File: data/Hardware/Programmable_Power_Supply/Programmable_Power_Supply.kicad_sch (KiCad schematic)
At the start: 1 part, among them U1 STM32G431CBT6

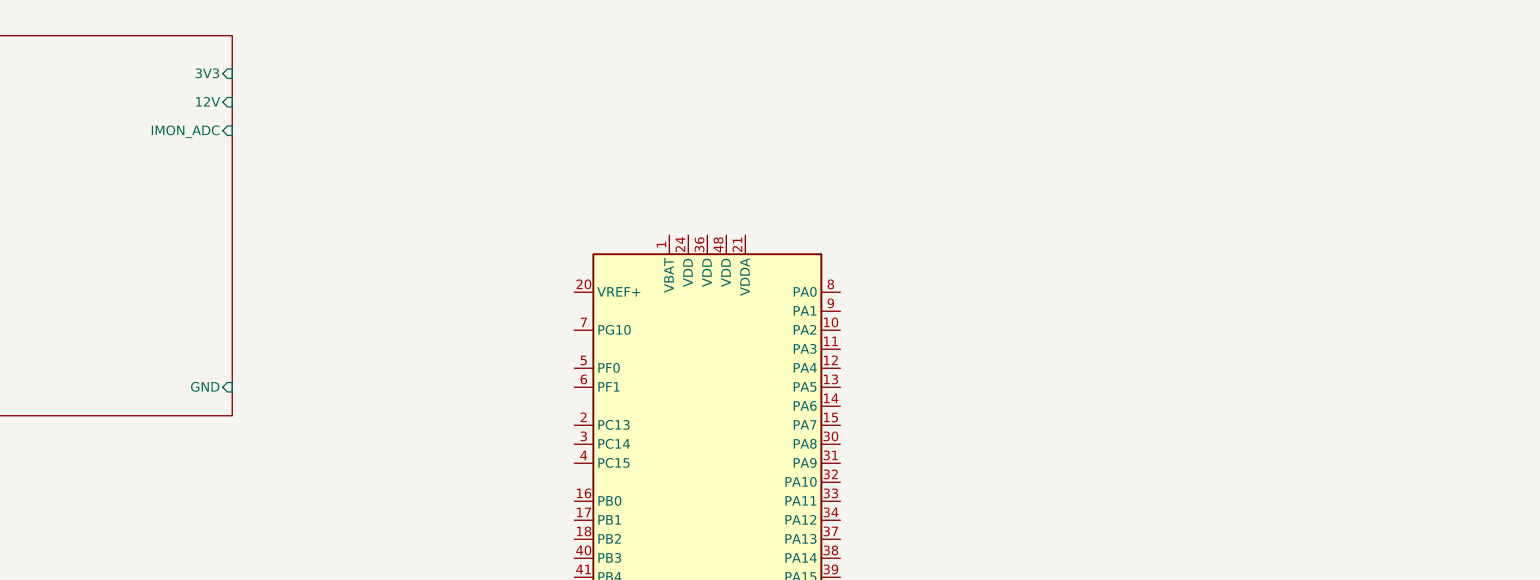
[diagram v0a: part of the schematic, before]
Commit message: feat: Adding output section to the schematic.
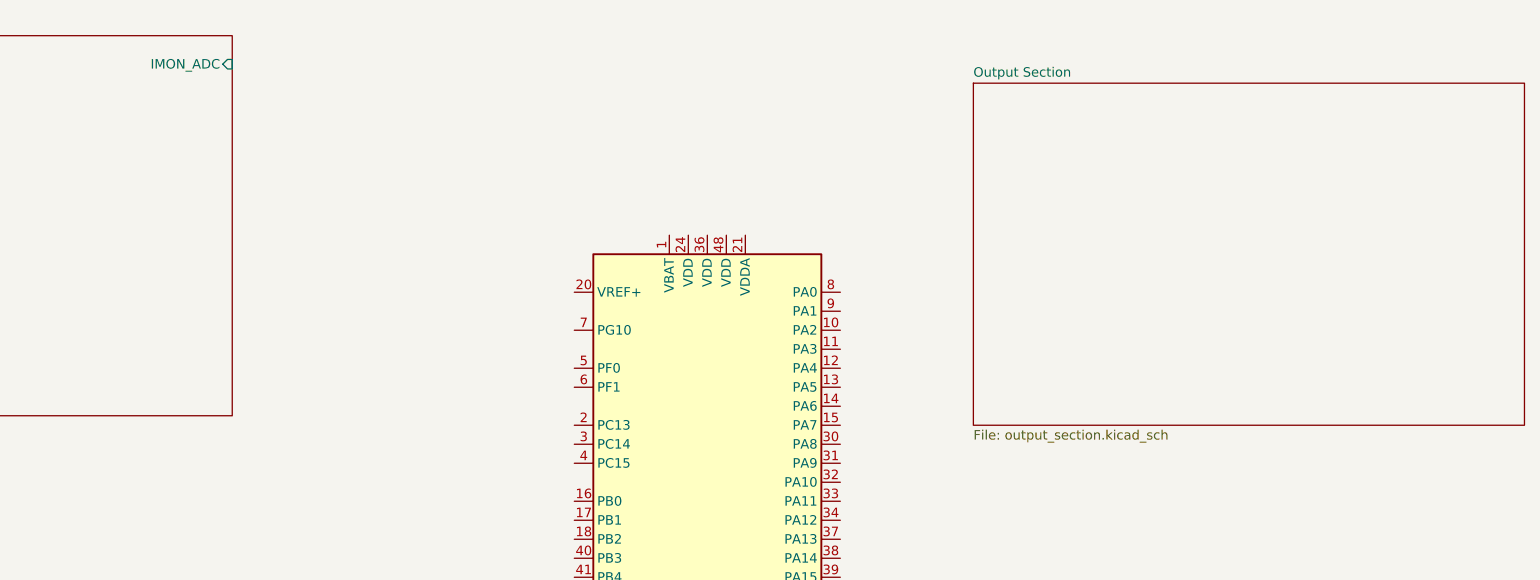
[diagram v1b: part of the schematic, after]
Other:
- added sheet Output Section (output_section.kicad_sch)
- sheet Input Section ports: added none; removed 12V, 3V3, GND
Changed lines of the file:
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@@
+	)
+	(sheet
+		(at 203.2 27.94)
+		(size 73.66 45.72)
+		(exclude_from_sim no)
+		(in_bom yes)
+		(on_board yes)
+		(dnp no)
+		(fields_autoplaced yes)
+		(stroke
+			(width 0.1524)
+			(type solid)
+		)
+		(fill
+			(color 0 0 0 0.0000)
+		)
+		(property "Sheetname" "Output Section"
+			(at 203.2 27.2284 0)
+			(effects
+				(font
+					(size 1.27 1.27)
+				)
+				(justify left bottom)
+			)
+		)
+		(property "Sheetfile" "output_section.kicad_sch"
+			(at 203.2 74.2446 0)
+			(effects
+				(font
+					(size 1.27 1.27)
+				)
+				(justify left top)
+			)
+		)
+		(instances
+			(project "Programmable_Power_Supply"
+				(path "/b54e5edd-9bd1-4c5e-a8c2-662f0aedeac0"
+					(page "3")
+				)
+			)
+		)
 	)
 	(sheet
@@
 			)
 		)
-		(pin "3V3" input
-			(at 104.14 26.67 0)
+		(pin "IMON_ADC" input
+			(at 104.14 25.4 0)
 			(effects
 				(font
-					(size 1.27 1.27)
-				)
-				(justify right)
-			)
-		)
-		(pin "12V" input
-			(at 104.14 30.48 0)
-			(effects
-				(font
-					(size 1.27 1.27)
-				)
-				(justify right)
-			)
-		)
-		(pin "GND" input
-			(at 104.14 68.58 0)
-			(effects
-				(font
-					(size 1.27 1.27)
-				)
-				(justify right)
-			)
-		)
-		(pin "IMON_ADC" input
-			(at 104.14 34.29 0)
-			(effects
-				(font

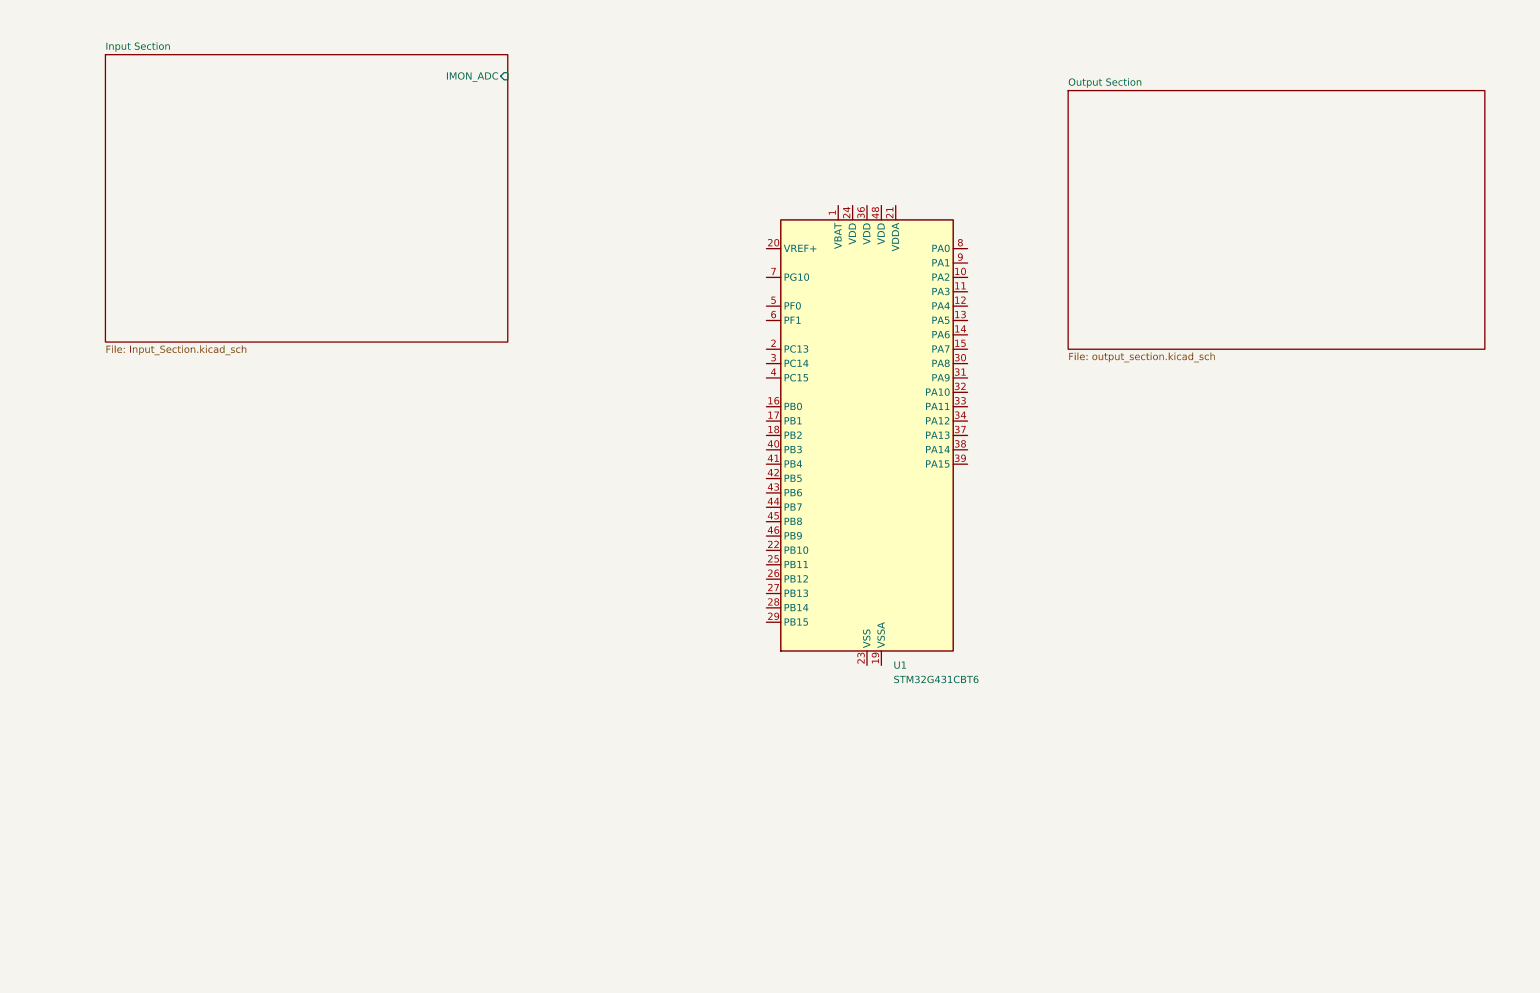
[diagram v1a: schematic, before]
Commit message: feat: First draw of full schematic with all footprints and symbols.
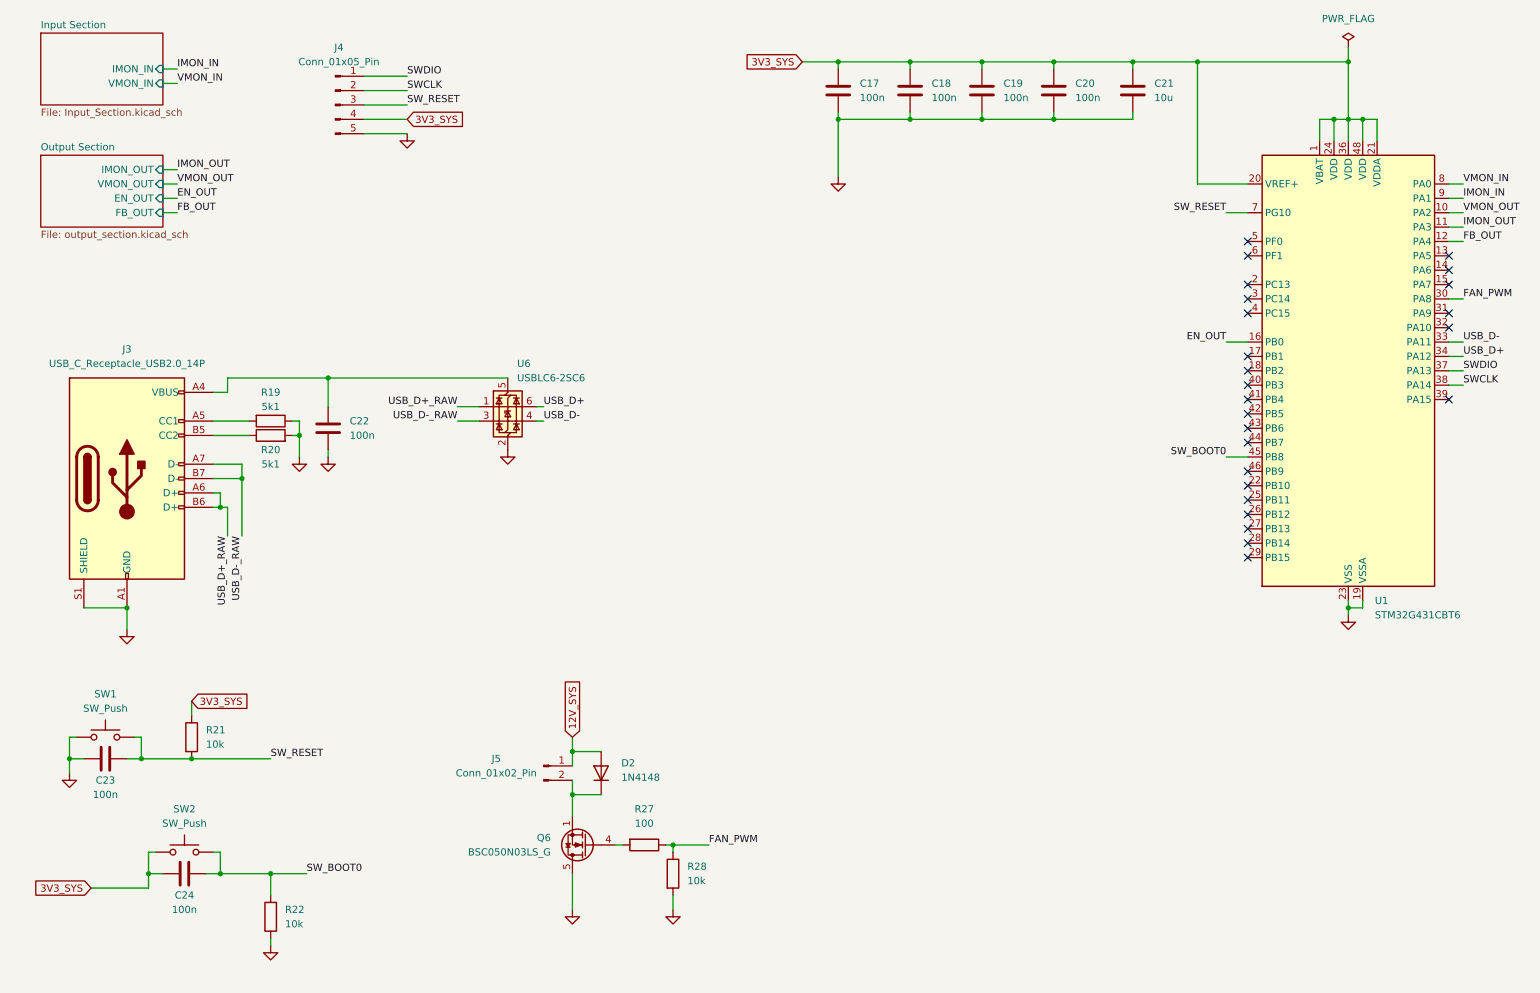
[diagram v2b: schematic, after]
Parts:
- added C17, C18, C19, C20, C22, C23, C24: 100n, Capacitor_SMD:C_0805_2012Metric_Pad1.18x1.45mm_HandSolder, symbol Device:C
- added C21: 10u, Capacitor_SMD:C_1206_3216Metric_Pad1.33x1.80mm_HandSolder, symbol Device:C
- added D2: 1N4148, Diode_THT:D_DO-35_SOD27_P7.62mm_Horizontal, symbol Diode:1N4148
- added J3: USB_C_Receptacle_USB2.0_14P, Connector_USB:USB_C_Receptacle_HRO_TYPE-C-31-M-12, symbol Connector:USB_C_Receptacle_USB2.0_14P
- added J4: Conn_01x05_Pin, Connector_PinHeader_2.54mm:PinHeader_1x05_P2.54mm_Vertical, symbol Connector:Conn_01x05_Pin
- added J5: Conn_01x02_Pin, Connector_Molex:Molex_KK-254_AE-6410-02A_1x02_P2.54mm_Vertical, symbol Connector:Conn_01x02_Pin
- added Q6: BSC050N03LS_G, Package_SON:Infineon_PG-TDSON-8_6.15x5.15mm, symbol Szymon_Piorun_library:BSC050N03LS_G
- added R19, R20: 5k1, Resistor_SMD:R_0603_1608Metric_Pad0.98x0.95mm_HandSolder, symbol Device:R
- added R21, R22, R28: 10k, Resistor_SMD:R_0603_1608Metric_Pad0.98x0.95mm_HandSolder, symbol Device:R
- added R27: 100, Resistor_SMD:R_0603_1608Metric_Pad0.98x0.95mm_HandSolder, symbol Device:R
- added SW1, SW2: SW_Push, Button_Switch_SMD:SW_Push_1P1T_NO_CK_KSC6xxG, symbol Switch:SW_Push
- added U6: USBLC6-2SC6, Package_TO_SOT_SMD:SOT-23-6, symbol Power_Protection:USBLC6-2SC6
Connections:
- net 3V3_SYS: now reaches U1.1 (VBAT)
- net 3V3_SYS: now also U1.20 (VREF+), U1.21 (VDDA), U1.24 (VDD), U1.36 (VDD), U1.48 (VDD), C17.1, C18.1, C19.1, C20.1, C21.1, C24.2, J4.4 (Pin_4), R21.1, SW2.1
- net VMON_OUT: now reaches U1.10 (PA2)
- net IMON_OUT: now reaches U1.11 (PA3)
- net FB_OUT: now reaches U1.12 (PA4)
- net EN_OUT: now reaches U1.16 (PB0)
- net GND: now reaches U1.19 (VSSA)
- net GND: now also U1.23 (VSS), U1.35 (VSS), U1.47 (VSS), C17.2, C18.2, C19.2, C20.2, C21.2, C22.2, C23.2, J3.A1 (GND), J3.A12 (GND), J3.B1 (GND), J3.B12 (GND), J3.S1 (SHIELD), J4.5 (Pin_5), Q6.5 (D), Q6.6 (D), Q6.7 (D), Q6.8 (D), R19.1, R20.2, R22.1, R28.2, SW1.1, U6.2 (GND)
- net FAN_PWM: now reaches U1.30 (PA8)
- net FAN_PWM: now also R27.1, R28.1
- net USB_D-: now reaches U1.33 (PA11)
- net USB_D-: now also U6.4 (I/O2)
- net USB_D+: now reaches U1.34 (PA12)
- net USB_D+: now also U6.6 (I/O1)
- net SWDIO: now reaches U1.37 (PA13)
- net SWDIO: now also J4.1 (Pin_1)
- net SWCLK: now reaches U1.38 (PA14)
- net SWCLK: now also J4.2 (Pin_2)
- net SW_BOOT0: now reaches U1.45 (PB8)
- net SW_BOOT0: now also C24.1, R22.2, SW2.2
- net SW_RESET: now reaches U1.7 (PG10)
- net SW_RESET: now also C23.1, J4.3 (Pin_3), R21.2, SW1.2
- net VMON_IN: now reaches U1.8 (PA0)
- net IMON_IN: now reaches U1.9 (PA1)
- new net: C22.1, J3.A4 (VBUS), J3.A9 (VBUS), J3.B4 (VBUS), J3.B9 (VBUS), U6.5 (VBUS)
- new net: J3.A5 (CC1), R19.2
- new net: D2.1 (K), J5.2 (Pin_2), Q6.1 (S), Q6.2 (S), Q6.3 (S)
- new net: Q6.4 (G), R27.2
- new net: J3.B5 (CC2), R20.1
- new net 12V_SYS: D2.2 (A), J5.1 (Pin_1)
- new net USB_D+_RAW: J3.A6 (D+), J3.B6 (D+), U6.1 (I/O1)
- new net USB_D-_RAW: J3.A7 (D-), J3.B7 (D-), U6.3 (I/O2)
- no-connect marks 0 -> 25
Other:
- sheet Input Section ports: added IMON_IN, VMON_IN; removed IMON_ADC
- sheet Output Section ports: added EN_OUT, FB_OUT, IMON_OUT, VMON_OUT; removed none
- moved on the sheet: U1

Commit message: feat: Final version of revision A of the schematic with mouser product numbers attached.
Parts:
- removed J3: USB_C_Receptacle_USB2.0_14P, Connector_USB:USB_C_Receptacle_HRO_TYPE-C-31-M-12, symbol Connector:USB_C_Receptacle_USB2.0_14P
- added J6: USB_C_Receptacle_USB2.0_16P, Connector_USB:USB_C_Receptacle_GCT_USB4105-xx-A_16P_TopMnt_Horizontal, symbol Connector:USB_C_Receptacle_USB2.0_16P
- C17, C18, C19, C20, C22, C23, C24: footprint Capacitor_SMD:C_0805_2012Metric_Pad1.18x1.45mm_HandSolder -> Capacitor_SMD:C_0201_0603Metric_Pad0.64x0.40mm_HandSolder; Mouser (none) -> MLASG063SB5104KFNA01
- C21: Mouser (none) -> GXT31CR6YA106KE01L
- D2: footprint Diode_THT:D_DO-35_SOD27_P7.62mm_Horizontal -> Szymon_Piorun_Library:SOD323; Mouser (none) -> 1N4148WS-HE3_A-18
- J4: now left out of the parts list
- J5: Mouser (none) -> 22-23-2021
- Q6: footprint Package_SON:Infineon_PG-TDSON-8_6.15x5.15mm -> Szymon_Piorun_Library:Infineon_PG-TDSON-8_6.15x5.15mm; Mouser (none) -> BSC030N03LS G
- R19, R20: Mouser (none) -> CR0603-FX-5101ELF
- R21, R22, R28: Mouser (none) -> RCA060310K0FKEC
- R27: Mouser (none) -> RT0603BRB07100RL
- SW1, SW2: footprint Button_Switch_SMD:SW_Push_1P1T_NO_CK_KSC6xxG -> Szymon_Piorun_Library:TS046650BK100SMTTR; Mouser (none) -> TS04-66-50-BK-100-SMT-TR
- U1: Mouser (none) -> STM32G431CBT6
- U6: Mouser (none) -> USBLC6-2SC6
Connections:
- net GND: now also C23.1, R20.1, R22.2, J6.A1 (GND), J6.A12 (GND), J6.B1 (GND), J6.B12 (GND), J6.S1 (SHIELD); no longer C23.2, R20.2, R22.1
- net SW_BOOT0: now also R22.1; no longer R22.2
- net SW_RESET: now also C23.2; no longer C23.1
- net USB_D+_RAW: now also J6.A6 (D+), J6.B6 (D+)
- net USB_D-_RAW: now also J6.A7 (D-), J6.B7 (D-)
- net at C22.1, U6.5 (VBUS): now also J6.A4 (VBUS), J6.A9 (VBUS), J6.B4 (VBUS), J6.B9 (VBUS)
- net at R19.2: now also J6.A5 (CC1)
- new net: J6.B5 (CC2), R20.2
- no-connect marks 25 -> 27

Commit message: feat: First full layout of the PCB
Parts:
- added H1, H2, H3, H4: MH, MountingHole:MountingHole_3.2mm_M3_ISO7380_Pad_TopBottom, symbol Mechanical:MountingHole_Pad
- J4: value Conn_01x05_Pin -> SWD Debugging Port
- J5: value Conn_01x02_Pin -> Two Pin Fan Header
- Q6: Mouser BSC030N03LS G -> (none)
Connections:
- net FAN_PWM: now also U1.13 (PA5); no longer U1.30 (PA8)
- net GND: now also Q6.1 (S), Q6.2 (S), Q6.3 (S), H1.1, H2.1, H3.1, H4.1; no longer Q6.5 (D), Q6.6 (D), Q6.7 (D), Q6.8 (D)
- new net: D2.1 (K), J5.2 (Pin_2), Q6.5 (D)
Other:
- note added: "Cooling Fan"
- note added: "Debugging Port"
- note added: "Microcontroller"
- note added: "Mounting Holes"
- note added: "Reset and Boot switches"
- note added: "USB-C Connector"
- moved on the sheet: C17, C18, C19, C20, C21, C22, C23, D2, J4, J5, J6, R19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

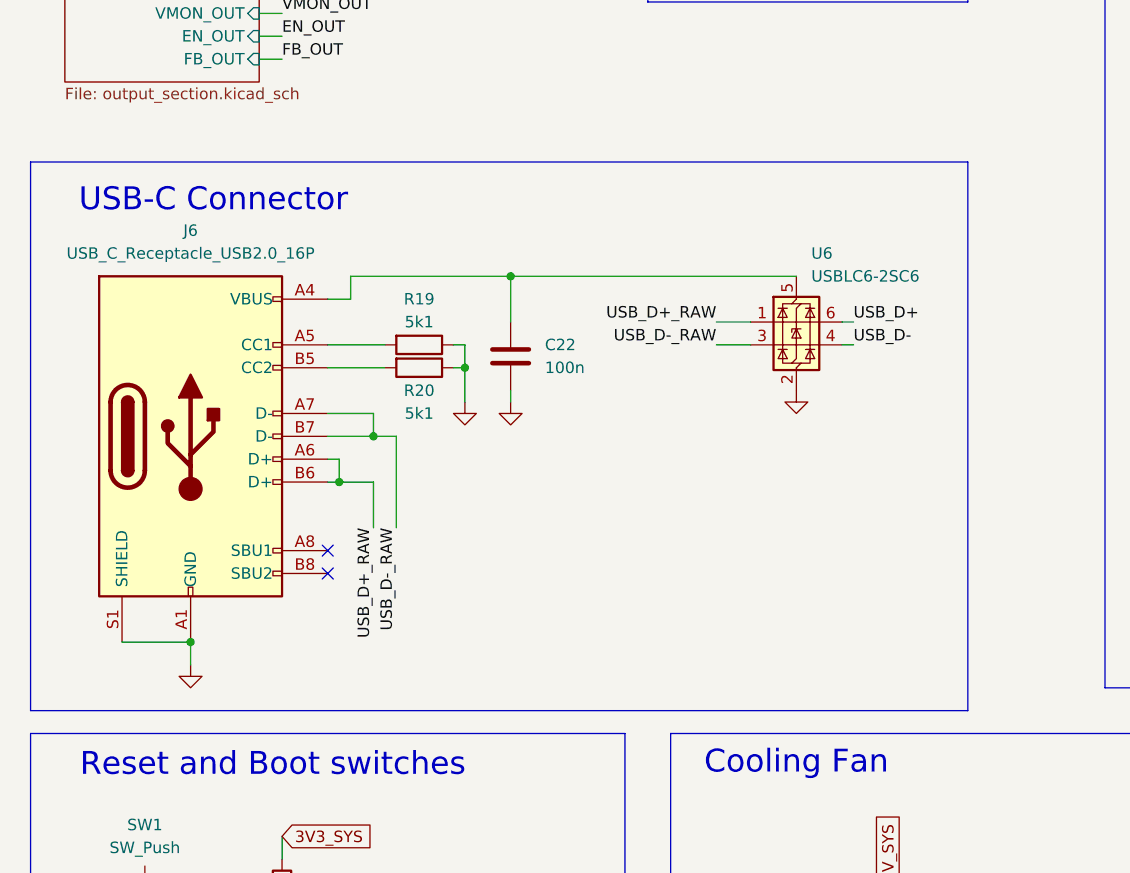
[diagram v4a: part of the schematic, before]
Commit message: feat: Layout of USB-C port and final beta version of the board.
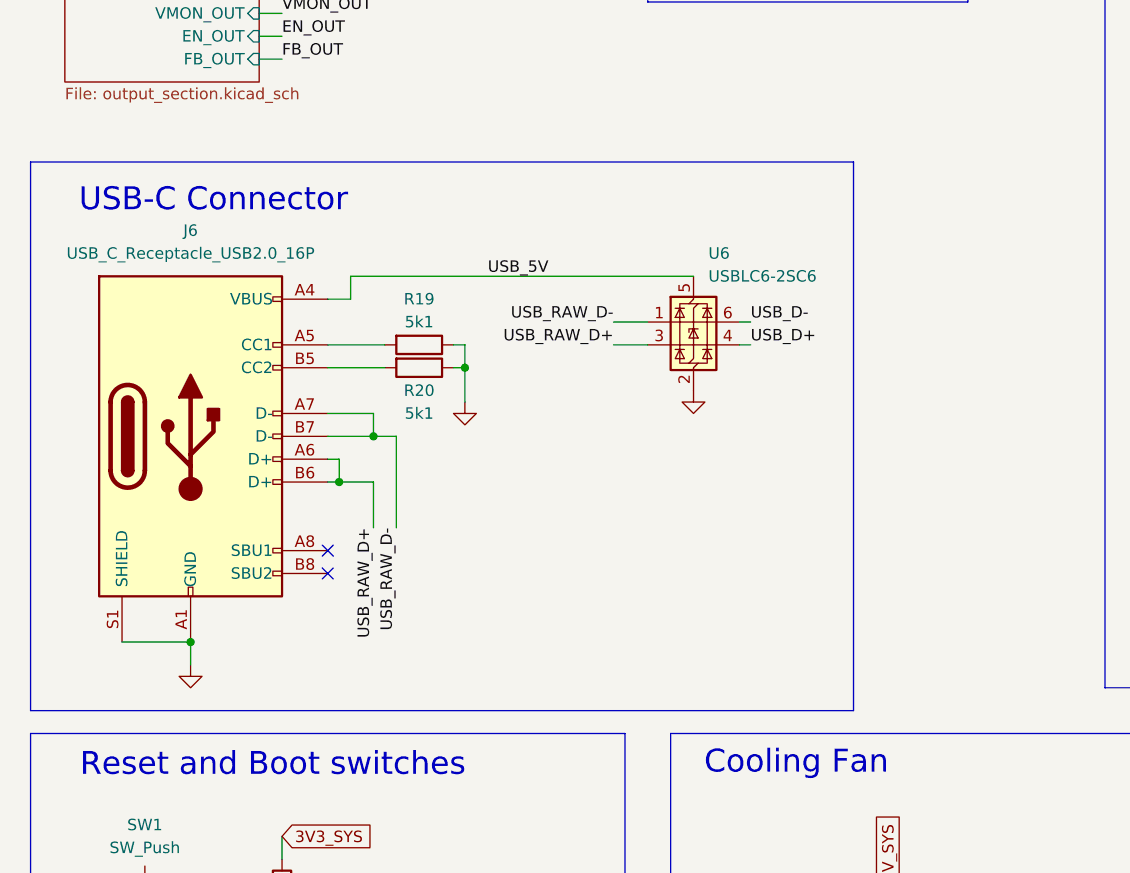
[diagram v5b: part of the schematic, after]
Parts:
- removed C22: 100n, Capacitor_SMD:C_0201_0603Metric_Pad0.64x0.40mm_HandSolder, symbol Device:C
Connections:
- net USB_D+: now also U6.4 (I/O2); no longer U6.6 (I/O1)
- net USB_D-: now also U6.6 (I/O1); no longer U6.4 (I/O2)
- net USB_5V: now reaches J6.A4 (VBUS), J6.A9 (VBUS), J6.B4 (VBUS), J6.B9 (VBUS), U6.5 (VBUS)
- net USB_D+_RAW renamed USB_RAW_D+
- net USB_RAW_D+: now also U6.3 (I/O2); no longer U6.1 (I/O1)
- net USB_D-_RAW renamed USB_RAW_D-
- net USB_RAW_D-: now also U6.1 (I/O1); no longer U6.3 (I/O2)
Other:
- moved on the sheet: U6
